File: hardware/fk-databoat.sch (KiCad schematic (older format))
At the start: 17 parts, among them P1 CONN_01X03, P2 CONN_01X03, P3 CONN_01X03, P4 CONN_01X03, P5 CONN_01X03, U1 VISO, U10 SERIAL_PORT_EXPANDER, U11 ATLAS_SENSOR, U12 ULTIMATE_GPS, U2 FEATHER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

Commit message: Starting to lay down traces.
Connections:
- net labels added: INT_SEL_1
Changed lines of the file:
@@
 INT_SEL_0
 Text Label 4900 1200 0    60   ~ 0
-INT_SEL_0
+INT_SEL_1
 Wire Wire Line
 	4900 1200 5350 1200
@@
 EC_RX
 Text Label 8600 4500 0    60   ~ 0
-EC_RX
+EC_TX
 Text Label 8600 4400 0    60   ~ 0
 EC_RX

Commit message: Last of the routing. Gonna do the cap on the solar charger now.
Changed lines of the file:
@@
 INT_SEL_0
 Text Label 4250 1300 0    60   ~ 0
-INT_SEL_0
+INT_SEL_1
 Text Label 4900 1100 0    60   ~ 0
 INT_SEL_0

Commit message: Add solar charger that pulls out some connections to slim things up.
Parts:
- removed U8: adafruit-solar-charger, conservify:adafruit-solar-charger, symbol adafruit-solar-charger
- added J1, J2: CONN_01X02, Socket_Strips:Socket_Strip_Straight_1x02_Pitch2.54mm, symbol CONN_01X02
- added U8: adafruit-solar-charger-with-cap, conservify:adafruit-solar-charger-with-cap, symbol adafruit-solar-charger-with-cap
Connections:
- wire segments 95 -> 99
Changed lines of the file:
@@
 ISO_V
 $Comp
-L GND #PWR01
+L GND #PWR4
 U 1 1 5887F11A
 P 2200 1000
-F 0 "#PWR01" H 2200 750 50  0001 C CNN
+F 0 "#PWR4" H 2200 750 50  0001 C CNN
 F 1 "GND" H 2200 850 50  0000 C CNN
 F 2 "" H 2200 1000 50  0000 C CNN
@@
 NoConn ~ 3250 3300
 $Comp
-L GND #PWR02
+L GND #PWR2
 U 1 1 5887FCB1
 P 1600 3100
-F 0 "#PWR02" H 1600 2850 50  0001 C CNN
+F 0 "#PWR2" H 1600 2850 50  0001 C CNN
 F 1 "GND" H 1600 2950 50  0000 C CNN
 F 2 "" H 1600 3100 50  0000 C CNN
@@
 NoConn ~ 1900 3000
 $Comp
-L +3V3 #PWR03
+L +3V3 #PWR1
 U 1 1 58880076
 P 1550 2900
-F 0 "#PWR03" H 1550 2750 50  0001 C CNN
+F 0 "#PWR1" H 1550 2750 50  0001 C CNN
 F 1 "+3V3" H 1550 3040 50  0000 C CNN
 F 2 "" H 1550 2900 50  0000 C CNN
@@
 	3900 3600 3250 3600
 $Comp
-L adafruit-solar-charger U8
-U 1 1 58D404A5
-P 2100 6800
-F 0 "U8" H 2000 6900 60  0000 C CNN
-F 1 "adafruit-solar-charger" H 2100 6800 60  0000 C CNN
-F 2 "conservify:adafruit-solar-charger" H 2100 6800 60  0001 C CNN
-F 3 "" H 2100 6800 60  0001 C CNN
-	1    2100 6800
-	-1   0    0    1
-$EndComp
-$Comp
 L FUELGUAGE U9
 U 1 1 58D40566
@@
 	4850 6000 4450 6000
 $Comp
-L GND #PWR04
+L GND #PWR7
 U 1 1 58D41093
 P 4500 6500
-F 0 "#PWR04" H 4500 6250 50  0001 C CNN
+F 0 "#PWR7" H 4500 6250 50  0001 C CNN
 F 1 "GND" H 4500 6350 50  0000 C CNN
 F 2 "" H 4500 6500 50  0000 C CNN
@@
 	3400 6950 3150 6950
 $Comp
-L GND #PWR05
+L GND #PWR5
 U 1 1 58D41AF4
 P 3550 6750
-F 0 "#PWR05" H 3550 6500 50  0001 C CNN
+F 0 "#PWR5" H 3550 6500 50  0001 C CNN
 F 1 "GND" H 3550 6600 50  0000 C CNN
 F 2 "" H 3550 6750 50  0000 C CNN
@@
 	3550 6750 3150 6750
 $Comp
-L +3V3 #PWR06
+L +3V3 #PWR3
 U 1 1 58D422F4
 P 2200 900
-F 0 "#PWR06" H 2200 750 50  0001 C CNN
+F 0 "#PWR3" H 2200 750 50  0001 C CNN
 F 1 "+3V3" H 2200 1040 50  0000 C CNN
 F 2 "" H 2200 900 50  0000 C CNN
@@
 $EndComp
 $Comp
-L +3V3 #PWR07
+L +3V3 #PWR9
 U 1 1 58F15EEB
 P 4950 4300
-F 0 "#PWR07" H 4950 4150 50  0001 C CNN
+F 0 "#PWR9" H 4950 4150 50  0001 C CNN
 F 1 "+3V3" H 4950 4440 50  0000 C CNN
 F 2 "" H 4950 4300 50  0000 C CNN
@@
 	4950 4400 5300 4400
 $Comp
-L GND #PWR08
+L GND #PWR8
 U 1 1 58F15F8E
 P 4850 4500
-F 0 "#PWR08" H 4850 4250 50  0001 C CNN
+F 0 "#PWR8" H 4850 4250 50  0001 C CNN
 F 1 "GND" H 4850 4350 50  0000 C CNN
 F 2 "" H 4850 4500 50  0000 C CNN
@@
 $EndComp
 $Comp
-L +3V3 #PWR09
+L +3V3 #PWR11
 U 1 1 58F16C59
 P 8500 4600
-F 0 "#PWR09" H 8500 4450 50  0001 C CNN
+F 0 "#PWR11" H 8500 4450 50  0001 C CNN
 F 1 "+3V3" H 8500 4740 50  0000 C CNN
 F 2 "" H 8500 4600 50  0000 C CNN
@@
 $EndComp
 $Comp
-L GND #PWR010
+L GND #PWR10
 U 1 1 58F16C91
 P 8250 4700
-F 0 "#PWR010" H 8250 4450 50  0001 C CNN
+F 0 "#PWR10" H 8250 4450 50  0001 C CNN
 F 1 "GND" H 8250 4550 50  0000 C CNN
 F 2 "" H 8250 4700 50  0000 C CNN
@@
 NoConn ~ 7350 4800
 $Comp
-L GND #PWR011
+L GND #PWR6
 U 1 1 58F17E69
 P 3750 4800
-F 0 "#PWR011" H 3750 4550 50  0001 C CNN
+F 0 "#PWR6" H 3750 4550 50  0001 C CNN
 F 1 "GND" H 3750 4650 50  0000 C CNN
 F 2 "" H 3750 4800 50  0000 C CNN
@@
 $EndComp
 $Comp
-L GND #PWR012
+L GND #PWR13
 U 1 1 58F1854D
 P 8600 5900
-F 0 "#PWR012" H 8600 5650 50  0001 C CNN
+F 0 "#PWR13" H 8600 5650 50  0001 C CNN
 F 1 "GND" H 8600 5750 50  0000 C CNN
 F 2 "" H 8600 5900 50  0000 C CNN
@@
 $EndComp
 $Comp
-L +3V3 #PWR013
+L +3V3 #PWR12
 U 1 1 58F1858B
 P 8600 5300
-F 0 "#PWR013" H 8600 5150 50  0001 C CNN
+F 0 "#PWR12" H 8600 5150 50  0001 C CNN
 F 1 "+3V3" H 8600 5440 50  0000 C CNN
 F 2 "" H 8600 5300 50  0000 C CNN
@@
 NoConn ~ 10750 1950
 NoConn ~ 10750 1200
+$Comp
+L adafruit-solar-charger-with-cap U8
+U 1 1 58F50108
+P 1900 6800
+F 0 "U8" H 1800 6900 60  0000 C CNN
+F 1 "adafruit-solar-charger-with-cap" H 1900 6800 60  0000 C CNN
+F 2 "conservify:adafruit-solar-charger-with-cap" H 1900 6800 60  0001 C CNN
+F 3 "" H 1900 6800 60  0001 C CNN
+	1    1900 6800
+	-1   0    0    1
+$EndComp
+$Comp
+L CONN_01X02 J1
+U 1 1 58F50394
+P 3700 6400
+F 0 "J1" H 3700 6550 50  0000 C CNN
+F 1 "CONN_01X02" V 3800 6400 50  0000 C CNN
+F 2 "Socket_Strips:Socket_Strip_Straight_1x02_Pitch2.54mm" H 3700 6400 50  0001 C CNN
+F 3 "" H 3700 6400 50  0001 C CNN
+	1    3700 6400
+	1    0    0    -1
+$EndComp
+Wire Wire Line
+	3150 6350 3500 6350
+Wire Wire Line
+	3500 6450 3150 6450
+$Comp
+L CONN_01X02 J2
+U 1 1 58F50E2D
+P 3450 6100
+F 0 "J2" H 3450 6250 50  0000 C CNN
+F 1 "CONN_01X02" V 3550 6100 50  0000 C CNN
+F 2 "Socket_Strips:Socket_Strip_Straight_1x02_Pitch2.54mm" H 3450 6100 50  0001 C CNN
+F 3 "" H 3450 6100 50  0001 C CNN
+	1    3450 6100
+	1    0    0    -1
+$EndComp
+Wire Wire Line
+	3250 6050 3150 6050
+Wire Wire Line
+	3150 6150 3250 6150
 $EndSCHEMATC

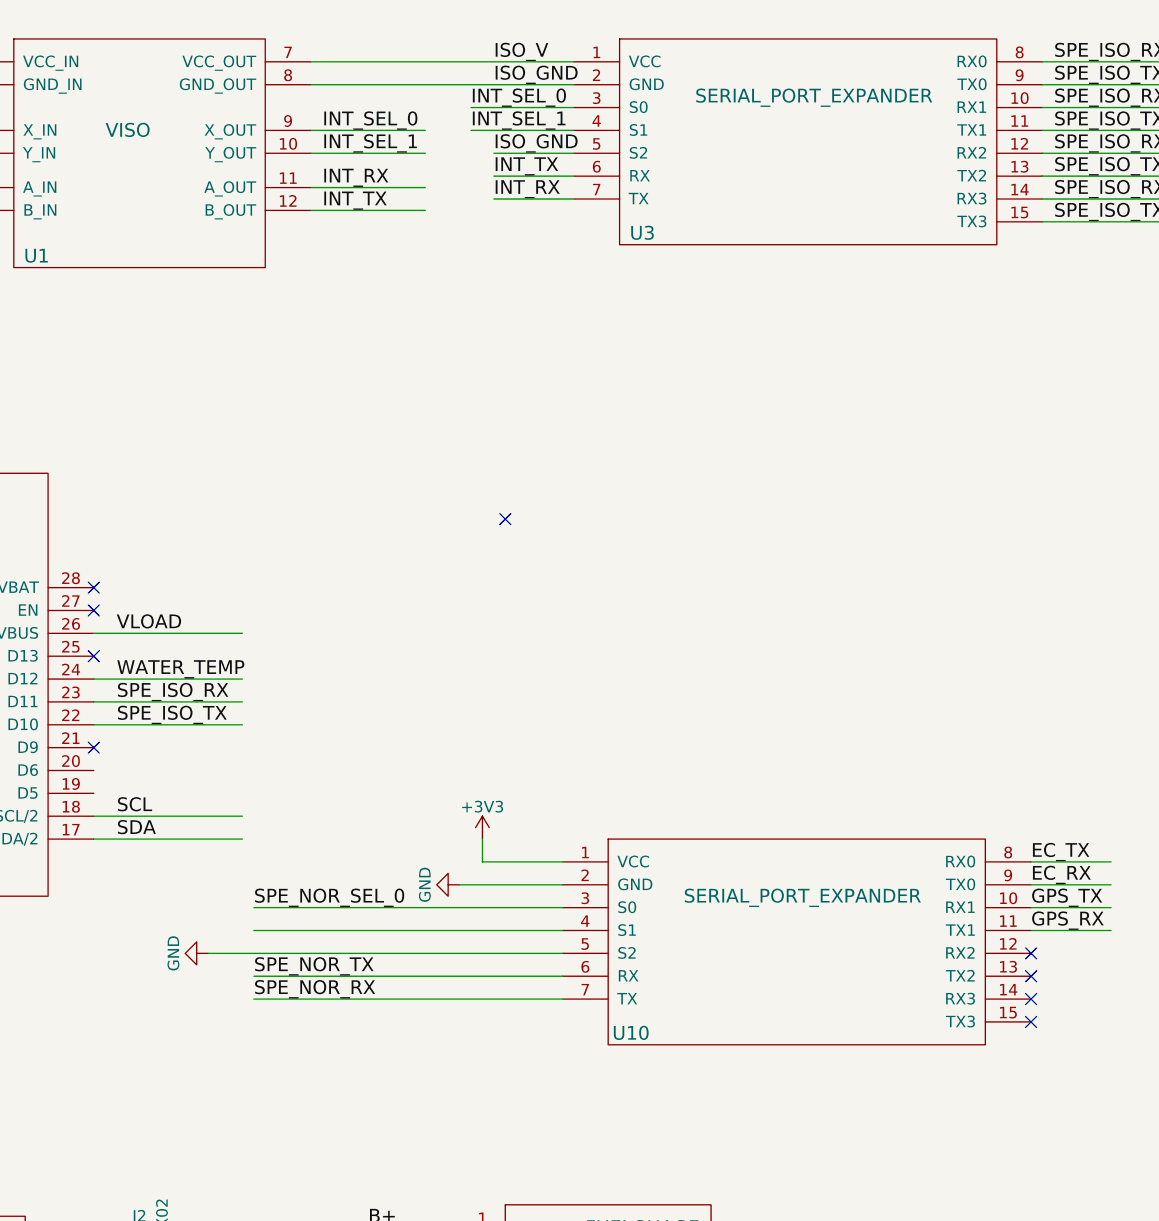
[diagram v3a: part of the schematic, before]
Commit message: Fix E and S1 GND issues on SPE. Add logo/version.
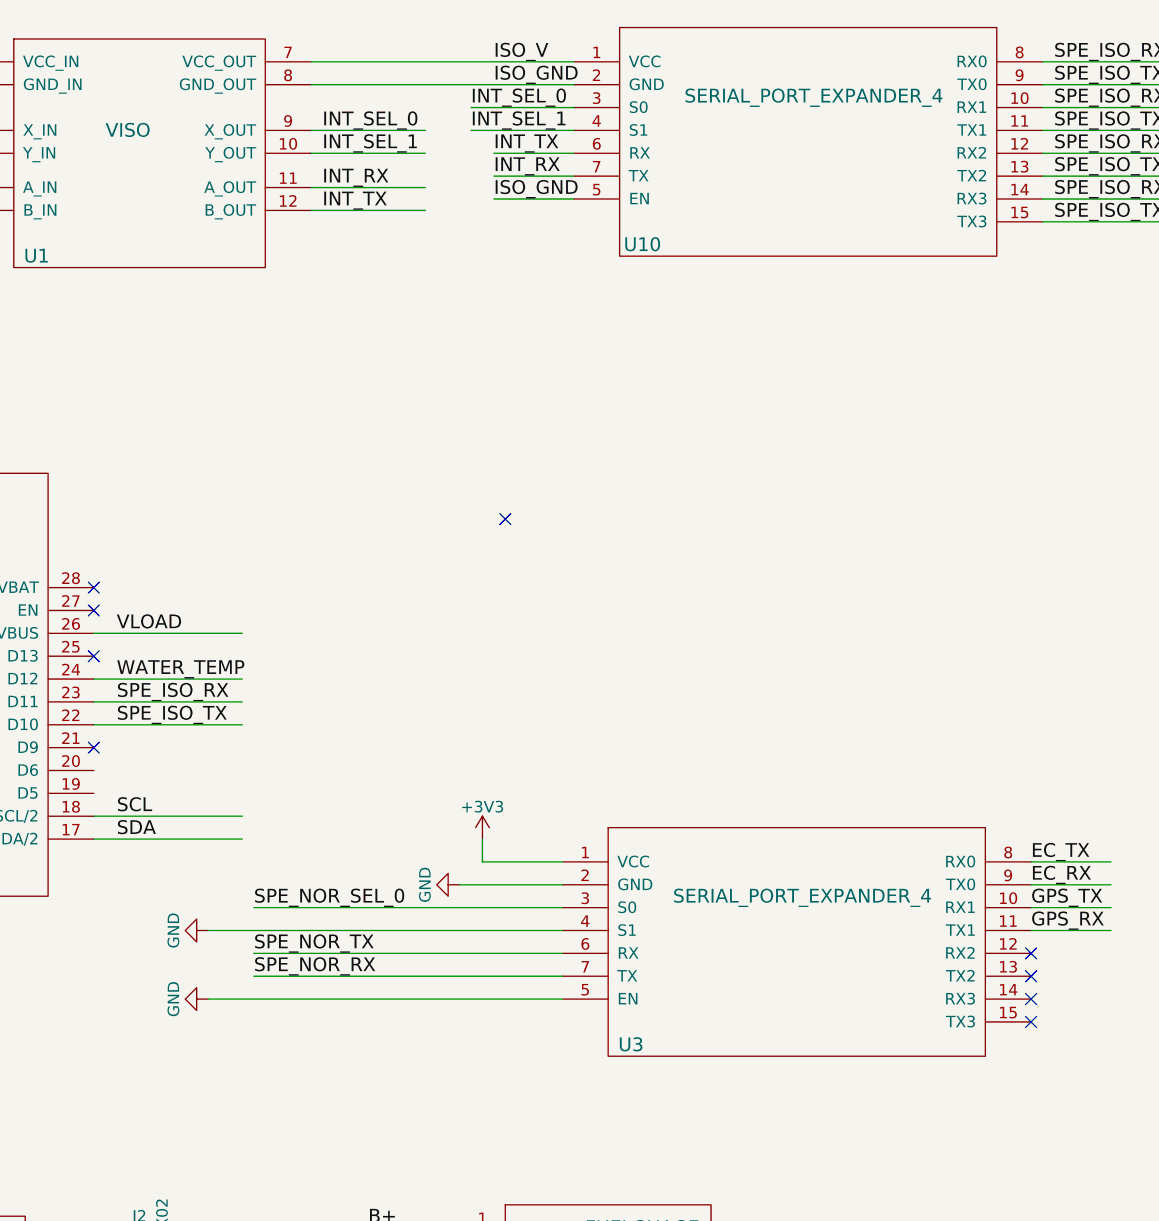
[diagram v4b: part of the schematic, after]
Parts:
- removed U10, U3: SERIAL_PORT_EXPANDER, conservify:serial_port_expander_small, symbol SERIAL_PORT_EXPANDER
- added U10, U3: SERIAL_PORT_EXPANDER_4, conservify:serial_port_expander_small, symbol SERIAL_PORT_EXPANDER_4
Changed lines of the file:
@@
 ISO_V
 $Comp
-L GND #PWR4
+L GND #PWR01
 U 1 1 5887F11A
 P 2200 1000
-F 0 "#PWR4" H 2200 750 50  0001 C CNN
+F 0 "#PWR01" H 2200 750 50  0001 C CNN
 F 1 "GND" H 2200 850 50  0000 C CNN
 F 2 "" H 2200 1000 50  0000 C CNN
@@
 NoConn ~ 3250 3300
 $Comp
-L GND #PWR2
+L GND #PWR02
 U 1 1 5887FCB1
 P 1600 3100
-F 0 "#PWR2" H 1600 2850 50  0001 C CNN
+F 0 "#PWR02" H 1600 2850 50  0001 C CNN
 F 1 "GND" H 1600 2950 50  0000 C CNN
 F 2 "" H 1600 3100 50  0000 C CNN
@@
 NoConn ~ 1900 3000
 $Comp
-L +3V3 #PWR1
+L +3V3 #PWR03
 U 1 1 58880076
 P 1550 2900
-F 0 "#PWR1" H 1550 2750 50  0001 C CNN
+F 0 "#PWR03" H 1550 2750 50  0001 C CNN
 F 1 "+3V3" H 1550 3040 50  0000 C CNN
 F 2 "" H 1550 2900 50  0000 C CNN
@@
 NoConn ~ 3250 3500
 NoConn ~ 3250 3900
-$Comp
-L SERIAL_PORT_EXPANDER U3
-U 1 1 58C69C65
-P 6400 1050
-F 0 "U3" H 5650 450 60  0000 C CNN
-F 1 "SERIAL_PORT_EXPANDER" H 6400 1050 60  0000 C CNN
-F 2 "conservify:serial_port_expander_small" H 6400 1050 60  0001 C CNN
-F 3 "" H 6400 1050 60  0001 C CNN
-	1    6400 1050
-	1    0    0    -1
-$EndComp
 Wire Wire Line
 	8500 1100 8900 1100
@@
 Text Label 3350 4300 0    60   ~ 0
 SDA
-Text Label 5000 1300 0    60   ~ 0
+Text Label 5000 1500 0    60   ~ 0
 ISO_GND
 Text Label 3350 3600 0    60   ~ 0
@@
 	4850 6000 4450 6000
 $Comp
-L GND #PWR7
+L GND #PWR04
 U 1 1 58D41093
 P 4500 6500
-F 0 "#PWR7" H 4500 6250 50  0001 C CNN
+F 0 "#PWR04" H 4500 6250 50  0001 C CNN
 F 1 "GND" H 4500 6350 50  0000 C CNN
 F 2 "" H 4500 6500 50  0000 C CNN
@@
 	3400 6950 3150 6950
 $Comp
-L GND #PWR5
+L GND #PWR05
 U 1 1 58D41AF4
 P 3550 6750
-F 0 "#PWR5" H 3550 6500 50  0001 C CNN
+F 0 "#PWR05" H 3550 6500 50  0001 C CNN
 F 1 "GND" H 3550 6600 50  0000 C CNN
 F 2 "" H 3550 6750 50  0000 C CNN
@@
 	3550 6750 3150 6750
 $Comp
-L +3V3 #PWR3
+L +3V3 #PWR06
 U 1 1 58D422F4
 P 2200 900
-F 0 "#PWR3" H 2200 750 50  0001 C CNN
+F 0 "#PWR06" H 2200 750 50  0001 C CNN
 F 1 "+3V3" H 2200 1040 50  0000 C CNN
 F 2 "" H 2200 900 50  0000 C CNN
@@
 NoConn ~ 4850 6300
 $Comp
-L SERIAL_PORT_EXPANDER U10
-U 1 1 58F15E7F
-P 6350 4550
-F 0 "U10" H 5600 3950 60  0000 C CNN
-F 1 "SERIAL_PORT_EXPANDER" H 6350 4550 60  0000 C CNN
-F 2 "conservify:serial_port_expander_small" H 6350 4550 60  0001 C CNN
-F 3 "" H 6350 4550 60  0001 C CNN
-	1    6350 4550
-	1    0    0    -1
-$EndComp
-$Comp
-L +3V3 #PWR9
+L +3V3 #PWR07
 U 1 1 58F15EEB
 P 4950 4300
-F 0 "#PWR9" H 4950 4150 50  0001 C CNN
+F 0 "#PWR07" H 4950 4150 50  0001 C CNN
 F 1 "+3V3" H 4950 4440 50  0000 C CNN
 F 2 "" H 4950 4300 50  0000 C CNN
@@
 	4950 4400 5300 4400
 $Comp
-L GND #PWR8
+L GND #PWR08
 U 1 1 58F15F8E
 P 4850 4500
-F 0 "#PWR8" H 4850 4250 50  0001 C CNN
+F 0 "#PWR08" H 4850 4250 50  0001 C CNN
 F 1 "GND" H 4850 4350 50  0000 C CNN
 F 2 "" H 4850 4500 50  0000 C CNN
@@
 	3950 4600 5300 4600
 Wire Wire Line
-	3950 4700 5300 4700
+	3750 4700 5300 4700
 Wire Wire Line
 	3950 4900 5300 4900
 Wire Wire Line
-	3950 5000 5300 5000
+	3750 5000 5300 5000
 $Comp
 L ATLAS_SENSOR U11
@@
 $EndComp
 $Comp
-L +3V3 #PWR11
+L +3V3 #PWR09
 U 1 1 58F16C59
 P 8500 4600
-F 0 "#PWR11" H 8500 4450 50  0001 C CNN
+F 0 "#PWR09" H 8500 4450 50  0001 C CNN
 F 1 "+3V3" H 8500 4740 50  0000 C CNN
 F 2 "" H 8500 4600 50  0000 C CNN
@@
 $EndComp
 $Comp
-L GND #PWR10
+L GND #PWR010
 U 1 1 58F16C91
 P 8250 4700
-F 0 "#PWR10" H 8250 4450 50  0001 C CNN
+F 0 "#PWR010" H 8250 4450 50  0001 C CNN
 F 1 "GND" H 8250 4550 50  0000 C CNN
 F 2 "" H 8250 4700 50  0000 C CNN
@@
 NoConn ~ 7350 4800
 $Comp
-L GND #PWR6
+L GND #PWR011
 U 1 1 58F17E69
-P 3750 4800
-F 0 "#PWR6" H 3750 4550 50  0001 C CNN
-F 1 "GND" H 3750 4650 50  0000 C CNN
-F 2 "" H 3750 4800 50  0000 C CNN
-F 3 "" H 3750 4800 50  0000 C CNN
-	1    3750 4800
+P 3750 5000
+F 0 "#PWR011" H 3750 4750 50  0001 C CNN
+F 1 "GND" H 3750 4850 50  0000 C CNN
+F 2 "" H 3750 5000 50  0000 C CNN
+F 3 "" H 3750 5000 50  0000 C CNN
+	1    3750 5000
 	0    1    1    0
 $EndComp
 Wire Wire Line
-	3750 4800 5300 4800
+	3950 4800 5300 4800
 $Comp
 L ULTIMATE_GPS U12
@@
 $EndComp
 $Comp
-L GND #PWR13
+L GND #PWR012
 U 1 1 58F1854D
 P 8600 5900
-F 0 "#PWR13" H 8600 5650 50  0001 C CNN
+F 0 "#PWR012" H 8600 5650 50  0001 C CNN
 F 1 "GND" H 8600 5750 50  0000 C CNN
 F 2 "" H 8600 5900 50  0000 C CNN
@@
 $EndComp
 $Comp
-L +3V3 #PWR12
+L +3V3 #PWR013
 U 1 1 58F1858B
 P 8600 5300
-F 0 "#PWR12" H 8600 5150 50  0001 C CNN
+F 0 "#PWR013" H 8600 5150 50  0001 C CNN
 F 1 "+3V3" H 8600 5440 50  0000 C CNN
 F 2 "" H 8600 5300 50  0000 C CNN
@@
 NoConn ~ 8900 6100
 NoConn ~ 5050 2900
+Text Label 3950 4800 0    60   ~ 0
+SPE_NOR_TX
 Text Label 3950 4900 0    60   ~ 0
-SPE_NOR_TX
-Text Label 3950 5000 0    60   ~ 0
 SPE_NOR_RX
 Text Label 7450 900  0    60   ~ 0
@@
 Text Label 4250 1550 0    60   ~ 0
 INT_TX
+Text Label 5000 1300 0    60   ~ 0
+INT_TX
 Text Label 5000 1400 0    60   ~ 0
-INT_TX
-Text Label 5000 1500 0    60   ~ 0
 INT_RX
 Wire Wire Line
@@
 Wire Wire Line
 	3150 6150 3250 6150
+$Comp
+L GND #PWR014
+U 1 1 59021EF3
+P 3750 4700
+F 0 "#PWR014" H 3750 4450 50  0001 C CNN
+F 1 "GND" H 3750 4550 50  0000 C CNN
+F 2 "" H 3750 4700 50  0000 C CNN
+F 3 "" H 3750 4700 50  0000 C CNN
+	1    3750 4700
+	0    1    1    0
+$EndComp
+$Comp
+L SERIAL_PORT_EXPANDER_4 U10
+U 1 1 59023D3F
+P 6400 1050
+F 0 "U10" H 5650 400 60  0000 C CNN
+F 1 "SERIAL_PORT_EXPANDER_4" H 6400 1050 60  0000 C CNN
+F 2 "conservify:serial_port_expander_small" H 6400 1050 60  0001 C CNN
+F 3 "" H 6400 1050 60  0001 C CNN
+	1    6400 1050
+	1    0    0    -1
+$EndComp
+$Comp
+L SERIAL_PORT_EXPANDER_4 U3
+U 1 1 59023E71
+P 6350 4550
+F 0 "U3" H 5600 3900 60  0000 C CNN
+F 1 "SERIAL_PORT_EXPANDER_4" H 6350 4550 60  0000 C CNN
+F 2 "conservify:serial_port_expander_small" H 6350 4550 60  0001 C CNN
+F 3 "" H 6350 4550 60  0001 C CNN
+	1    6350 4550
+	1    0    0    -1
+$EndComp
 $EndSCHEMATC

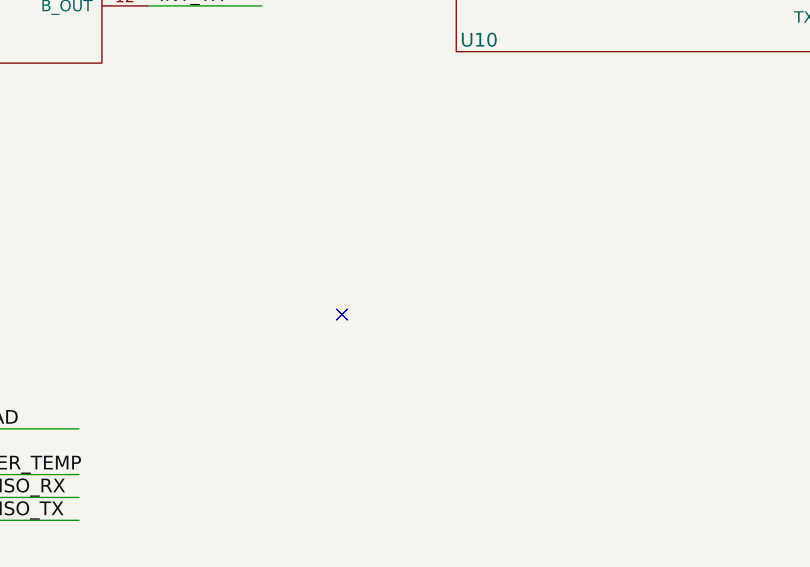
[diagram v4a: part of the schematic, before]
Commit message: Fixing GPS orientation.
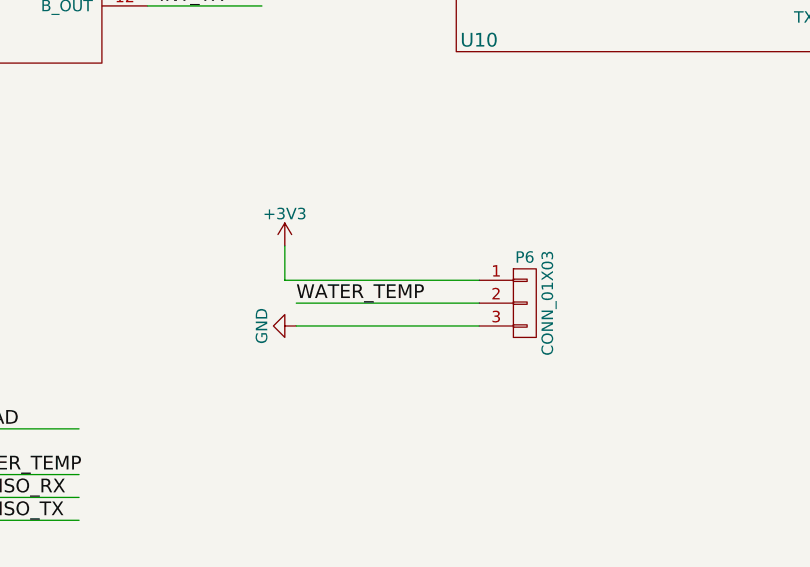
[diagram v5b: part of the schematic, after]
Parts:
- added P6: CONN_01X03, Socket_Strips:Socket_Strip_Straight_1x03_Pitch2.54mm, symbol CONN_01X03
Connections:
- wire segments 99 -> 103
- no-connect marks 27 -> 26
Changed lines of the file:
@@
 NoConn ~ 8900 6000
 NoConn ~ 8900 6100
-NoConn ~ 5050 2900
 Text Label 3950 4800 0    60   ~ 0
 SPE_NOR_TX
@@
 	1    0    0    -1
 $EndComp
+Text Label 4850 2850 0    60   ~ 0
+WATER_TEMP
+$Comp
+L CONN_01X03 P6
+U 1 1 5907B388
+P 5850 2850
+F 0 "P6" H 5850 3050 50  0000 C CNN
+F 1 "CONN_01X03" V 5950 2850 50  0000 C CNN
+F 2 "Socket_Strips:Socket_Strip_Straight_1x03_Pitch2.54mm" H 5850 2850 50  0001 C CNN
+F 3 "" H 5850 2850 50  0000 C CNN
+	1    5850 2850
+	1    0    0    -1
+$EndComp
+Wire Wire Line
+	5650 2850 4850 2850
+$Comp
+L GND #PWR015
+U 1 1 5907B66F
+P 4850 2950
+F 0 "#PWR015" H 4850 2700 50  0001 C CNN
+F 1 "GND" H 4850 2800 50  0000 C CNN
+F 2 "" H 4850 2950 50  0000 C CNN
+F 3 "" H 4850 2950 50  0000 C CNN
+	1    4850 2950
+	0    1    1    0
+$EndComp
+$Comp
+L +3V3 #PWR016
+U 1 1 5907B6B6
+P 4800 2600
+F 0 "#PWR016" H 4800 2450 50  0001 C CNN
+F 1 "+3V3" H 4800 2740 50  0000 C CNN
+F 2 "" H 4800 2600 50  0000 C CNN
+F 3 "" H 4800 2600 50  0000 C CNN
+	1    4800 2600
+	1    0    0    -1
+$EndComp
+Wire Wire Line
+	5650 2750 4800 2750
+Wire Wire Line
+	4800 2750 4800 2600
+Wire Wire Line
+	5650 2950 4850 2950
 $EndSCHEMATC
